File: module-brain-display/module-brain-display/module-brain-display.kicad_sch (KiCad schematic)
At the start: 19 parts, among them J1 Screw_Terminal_01x02, J2 Raspberry_Pi_2_3, J3 Conn_02x20_Top_Bottom, J4 Conn_01x16_Female, T1 Transformer_1P_1S, U1 LCD-016N002L, U2 L7805

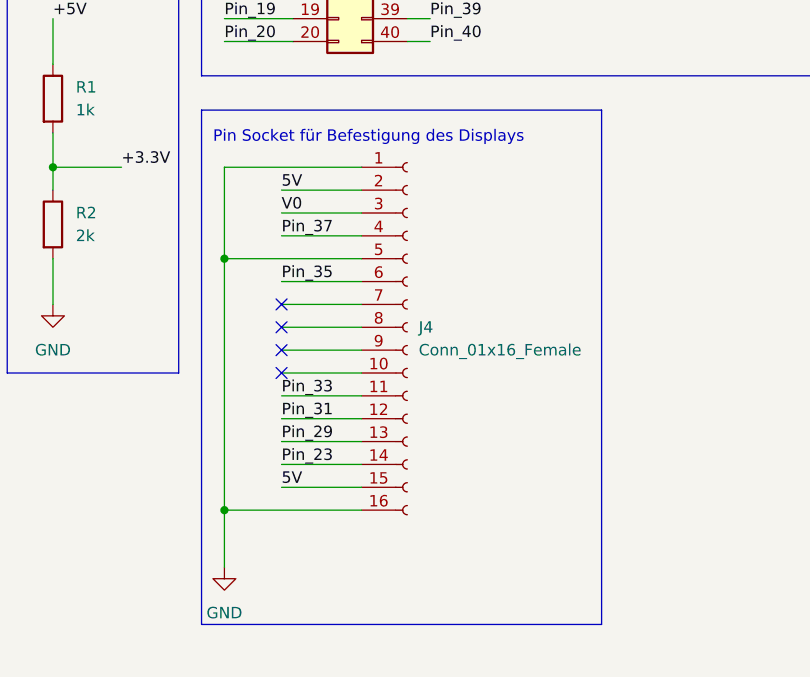
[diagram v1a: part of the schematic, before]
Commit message: KiCad 7.0
Updated to KiCad 7.0 file format
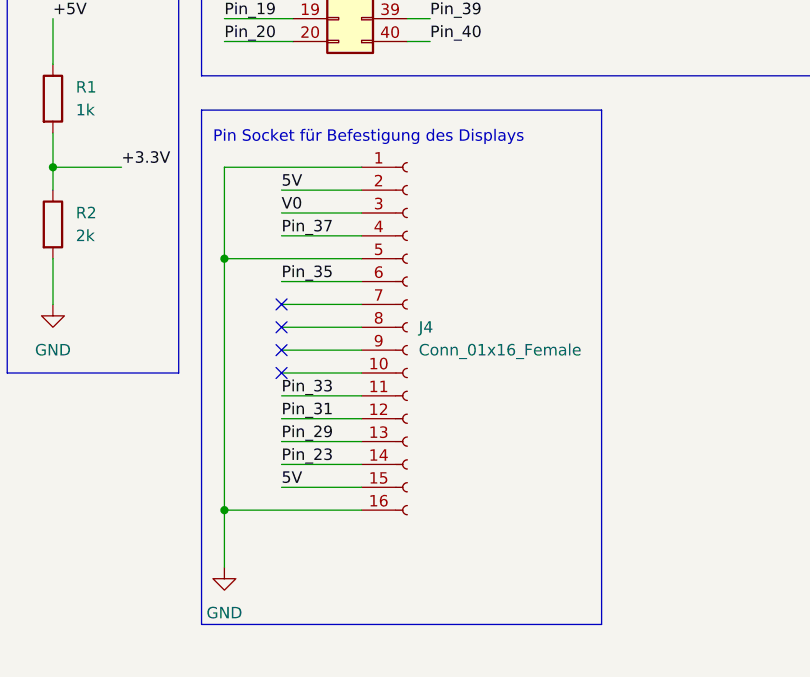
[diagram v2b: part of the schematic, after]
